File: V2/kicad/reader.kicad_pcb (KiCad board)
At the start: 2 copper layers, 42.5 x 62 mm, 93 parts, among them SW1 SW_Rezistance, SW2 SW_src, U1 STM32H523CET6, U2 MAX98357AETE+T, U3 MLD-TF PUSH-H18, U4 TCAN1057AVDRQ1, U5 ESD2CAN24-ES, U6 RJ-064-1, U7 MCP16301Hx-xCH, Y1 16MHz

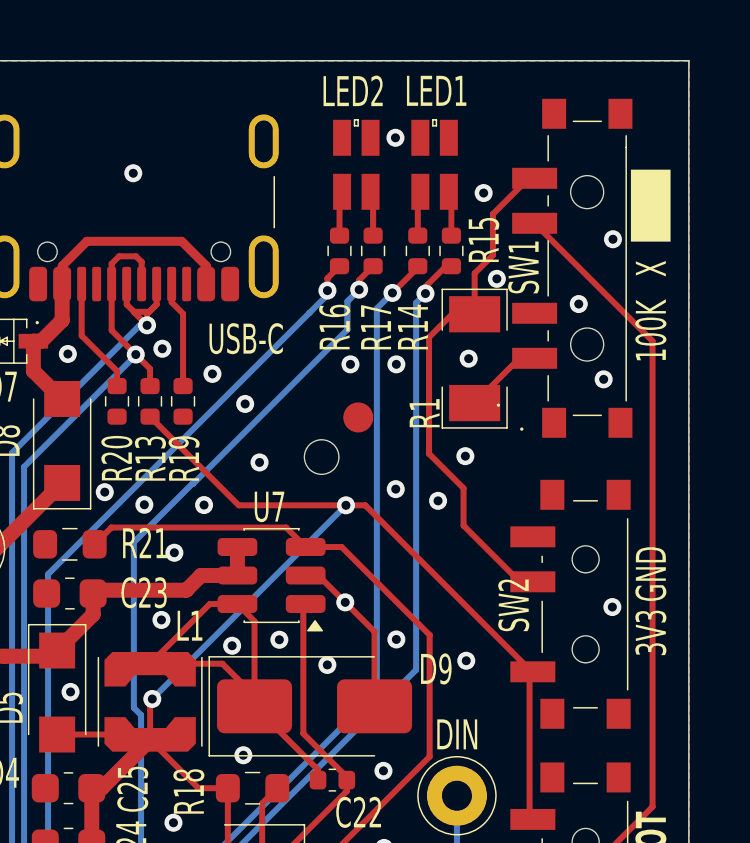
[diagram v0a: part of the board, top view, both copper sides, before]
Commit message: changed signage in gain slot table
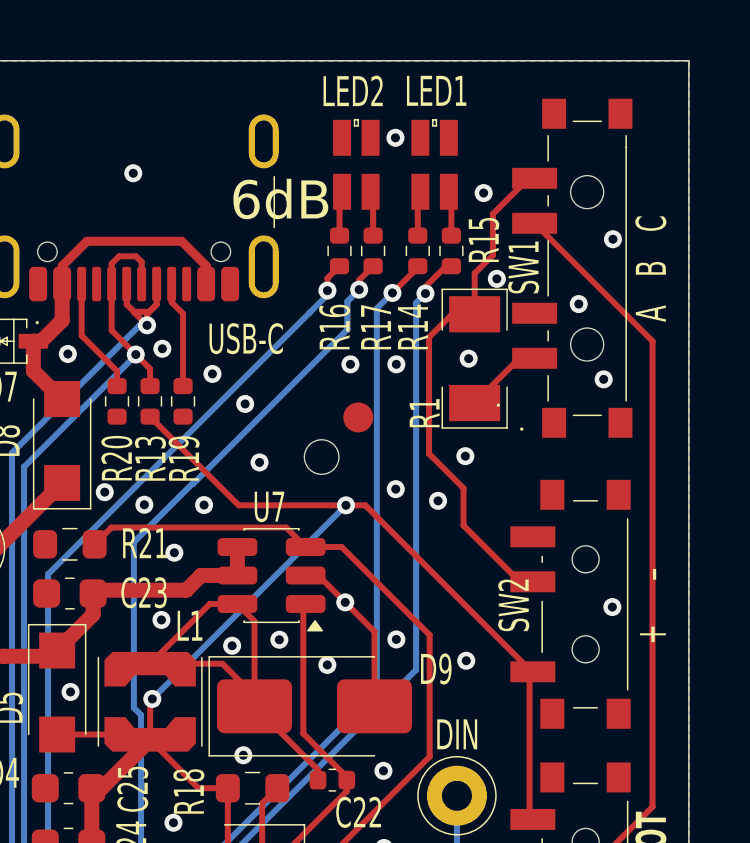
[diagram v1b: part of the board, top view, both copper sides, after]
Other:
- board text added: "+"
- board text added: "-"
- board text added: "6dB"
- board text added: "A"
- board text added: "B"
- board text added: "C"
- board text removed: "100K"
- board text removed: "3V3"
- board text removed: "GND"
- board text removed: "X"
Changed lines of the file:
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@@
 		(sheetname "/")
 		(sheetfile "reader.kicad_sch")
-		(units
-			(unit
-				(name "A")
-				(pins "2" "1" "3")
-			)
-		)
 		(attr smd)
 		(duplicate_pad_numbers_are_jumpers no)
@@
 		)
 		(fp_line
+			(start 0 3.4)
+			(end 0 1.6)
+			(stroke
+				(width 0.1)
+				(type default)
+			)
+			(layer "Dwgs.User")
+		)
+		(fp_line
 			(start 4.4 -2.45)
 			(end 4.4 2.1)
@@
 	)
 	(gr_rect
-		(start 173.5675 31.63)
-		(end 174.89 34.03)
-		(stroke
-			(width 0)
-			(type solid)
-		)
-		(fill yes)
-		(layer "F.SilkS")
-	)
-	(gr_rect
 		(start 136.36 63.09)
 		(end 136.84 73.86)
@@
 		(layer "Edge.Cuts")
 	)
-	(gr_text "X"
-		(at 174.27 34.93 90)
+	(gr_text "C"
+		(at 174.27 33.43 90)
 		(layer "F.SilkS" knockout)
 		(effects
@@
 		)
 	)
-	(gr_text "100K"
-		(at 174.27 37.02 90)
+	(gr_text "B"
+		(at 174.27 34.93 90)
 		(layer "F.SilkS" knockout)
 		(effects
@@
 		)
 	)
-	(gr_text "GND"
-		(at 174.27 45.11 90)
+	(gr_text "A"
+		(at 174.27 36.43 90)
 		(layer "F.SilkS" knockout)
 		(effects
@@
 		)
 	)
-	(gr_text "3V3\n"
-		(at 174.27 47.07 90)
+	(gr_text "+"
+		(at 174.27 47.119001 90)
 		(layer "F.SilkS" knockout)
 		(effects
@@
 		)
 	)
+	(gr_text "-"
+		(at 174.27 45.119001 90)
+		(layer "F.SilkS" knockout)
+		(effects
+			(font
+				(size 1 1)
+				(thickness 0.075)
+			)
+		)
+	)
+	(gr_text "6dB"
+		(at 161.9 32.67 0)
+		(layer "F.SilkS")
+		(effects
+			(font
+				(size 1.27 1.27)
+			)
+		)
+	)
 	(gr_text "https://github.com/ostertag/UACS"
 		(at 154.469519 65.849997 90)
@@
 	)
 	(table
-		(column_count 1)
+		(column_count 2)
 		(layer "B.SilkS")
 		(border
@@
 			)
 		)
-		(column_widths 16.306541)
-		(row_heights 3.15 3.15 4.225 3.15 3.15)
+		(column_widths 3.904256 5.767872)
+		(row_heights 3.15 3.15 3.15 3.15 3.15)
 		(cells
-			(table_cell "3dB = 3V3 100k"
-				(start 153.95 48.075)
-				(end 157.1 31.768459)
+			(table_cell "A+"
+				(start 155.425 46.096064)
+				(end 158.575 42.191808)
+				(margins 1.0025 1.0025 1.0025 1.0025)
+				(span 1 1)
+				(angle 90)
+				(layer "B.SilkS")
+				(effects
+					(font
+						(size 1 1)
+						(thickness 0.15)
+					)
+					(justify left mirror)
+				)
+			)
+			(table_cell "3dB\n"
+				(start 155.425 42.191808)
+				(end 158.575 36.423936)
 				(margins 1.0025 1.0025 1.0025 1.0025)
 				(span 1 1)
@@
 				)
 			)
-			(table_cell "6dB = 3V3"
-				(start 157.1 48.075)
-				(end 160.25 31.768459)
+			(table_cell "C+"
+				(start 158.575 46.096064)
+				(end 161.725 42.191808)
 				(margins 1.0025 1.0025 1.0025 1.0025)
 				(span 1 1)
@@
 				)
 			)
-			(table_cell "6dB = X"
-				(start 160.25 48.075)
-				(end 164.475 31.768459)
+			(table_cell "6dB"
+				(start 158.575 42.191808)
+				(end 161.725 36.423936)
 				(margins 1.0025 1.0025 1.0025 1.0025)
 				(span 1 1)
@@
 						(thickness 0.15)
 					)
-					(justify left bottom mirror)
+					(justify left mirror)
 				)
 			)
-			(table_cell "12dB = GND"
-				(start 164.475 48.075)
-				(end 167.625 31.768459)
+			(table_cell "B"
+				(start 161.725 46.096064)
+				(end 164.875 42.191808)
 				(margins 1.0025 1.0025 1.0025 1.0025)
 				(span 1 1)
@@
 				)
 			)
-			(table_cell "15dB = GND 100k"
-				(start 167.625 48.075)
-				(end 170.775 31.768459)
+			(table_cell "6dB"
+				(start 161.725 42.191808)
+				(end 164.875 36.423936)
+				(margins 1.0025 1.0025 1.0025 1.0025)
+				(span 1 1)
+				(angle 90)
+				(layer "B.SilkS")
+				(effects
+					(font
+						(size 1 1)
+						(thickness 0.15)
+					)
+					(justify left mirror)
+				)
+			)
+			(table_cell "C-"
+				(start 164.875 46.096064)
+				(end 168.025 42.191808)
+				(margins 1.0025 1.0025 1.0025 1.0025)
+				(span 1 1)
+				(angle 90)
+				(layer "B.SilkS")
+				(effects
+					(font
+						(size 1 1)
+						(thickness 0.15)
+					)
+					(justify left mirror)
+				)
+			)
+			(table_cell "12dB"
+				(start 164.875 42.191808)
+				(end 168.025 36.423936)
+				(margins 1.0025 1.0025 1.0025 1.0025)
+				(span 1 1)
+				(angle 90)
+				(layer "B.SilkS")
+				(effects
+					(font
+						(size 1 1)
+						(thickness 0.15)
+					)
+					(justify left mirror)
+				)
+			)
+			(table_cell "A-"
+				(start 168.025 46.096064)
+				(end 171.175 42.191808)
+				(margins 1.0025 1.0025 1.0025 1.0025)
+				(span 1 1)
+				(angle 90)
+				(layer "B.SilkS")
+				(effects
+					(font
+						(size 1 1)
+						(thickness 0.15)
+					)
+					(justify left mirror)
+				)
+			)
+			(table_cell "15dB"
+				(start 168.025 42.191808)
+				(end 171.175 36.423936)
 				(margins 1.0025 1.0025 1.0025 1.0025)
 				(span 1 1)
@@
 	)
 	(segment
+		(start 138.01 74.95)
+		(end 136.54 74.95)
+		(width 0.2)
+		(layer "F.Cu")
+		(net "Net-(U1-VDDA)")
+	)
+	(segment
+		(start 138.65 75.59)
+		(end 138.01 74.95)
+		(width 0.2)
+		(layer "F.Cu")
+		(net "Net-(U1-VDDA)")
+	)
+	(segment
+		(start 139.43595 73.28595)
+		(end 139.43595 75.00095)
+		(width 0.3)
+		(layer "F.Cu")
+		(net "Net-(U1-VDDA)")
+	)
+	(segment
+		(start 139.7329 72.989)
+		(end 139.43595 73.28595)
+		(width 0.3)
+		(layer "F.Cu")
+		(net "Net-(U1-VDDA)")
+	)
+	(segment
+		(start 140.8036 72.989)
+		(end 139.7329 72.989)
+		(width 0.3)
+		(layer "F.Cu")
+		(net "Net-(U1-VDDA)")
+	)
+	(segment
+		(start 139.43595 75.00095)
+		(end 140.21 75.775)
+		(width 0.3)
+		(layer "F.Cu")
+		(net "Net-(U1-VDDA)")
+	)
+	(segment
+		(start 138.65 75.59)
+		(end 138.8469 75.59)
+		(width 0.2)
+		(layer "F.Cu")
+		(net "Net-(U1-VDDA)")
+	)
+	(segment
+		(start 138.8469 75.59)
+		(end 139.43595 75.00095)
+		(width 0.2)
+		(layer "F.Cu")
+		(net "Net-(U1-VDDA)")
+	)
+	(segment
 		(start 164.51 35.63)
 		(end 164.51 35.314)
@@
 		(net "Net-(LED2-A2)")
 	)
-	(segment
-		(start 138.01 74.95)
-		(end 136.54 74.95)
-		(width 0.2)
-		(layer "F.Cu")
-		(net "Net-(U1-VDDA)")
-	)
-	(segment
-		(start 138.65 75.59)
-		(end 138.01 74.95)
-		(width 0.2)
-		(layer "F.Cu")
-		(net "Net-(U1-VDDA)")
-	)
-	(segment
-		(start 139.43595 73.28595)
-		(end 139.43595 75.00095)
-		(width 0.3)
-		(layer "F.Cu")
-		(net "Net-(U1-VDDA)")
-	)
-	(segment
-		(start 139.7329 72.989)
-		(end 139.43595 73.28595)
-		(width 0.3)
-		(layer "F.Cu")
-		(net "Net-(U1-VDDA)")
-	)
-	(segment
-		(start 140.8036 72.989)
-		(end 139.7329 72.989)
-		(width 0.3)
-		(layer "F.Cu")
-		(net "Net-(U1-VDDA)")
-	)
-	(segment
-		(start 139.43595 75.00095)
-		(end 140.21 75.775)
-		(width 0.3)
-		(layer "F.Cu")
-		(net "Net-(U1-VDDA)")
-	)
-	(segment
-		(start 138.65 75.59)
-		(end 138.8469 75.59)
-		(width 0.2)
-		(layer "F.Cu")
-		(net "Net-(U1-VDDA)")
-	)
-	(segment
-		(start 138.8469 75.59)
-		(end 139.43595 75.00095)
-		(width 0.2)
-		(layer "F.Cu")
-		(net "Net-(U1-VDDA)")
-	)
 	(zone

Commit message: fixed errors in board check: courtyard overlaps with fiducials
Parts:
- moved H2 1.87 mm to (161.4, 41.4)
- moved C21 1.66 mm to (160.7, 84.2)
- moved REF** 1.63 mm to (163.4, 83.3)
- moved REF** 1.25 mm to (145.0, 83.3)
- moved REF** 1.05 mm to (163.4, 39.9)
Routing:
- net +3.3V: track 186.3 -> 184.5 mm
- net Net-(SW2-B): track 16.5 -> 15.8 mm
- net /SPI_SCK: track 29.5 -> 30.1 mm
- net Net-(R1-Pad1): track 2.62 -> 2.11 mm
- net GND: vias 183 -> 182

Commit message: chore: small PCB layout changes
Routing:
- net /I2S_SDO: track 31.9 -> 32.5 mm
- net /RFID_SS: track 19.8 -> 19.2 mm
- net GND: vias 182 -> 187
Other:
- board text removed: "6dB"

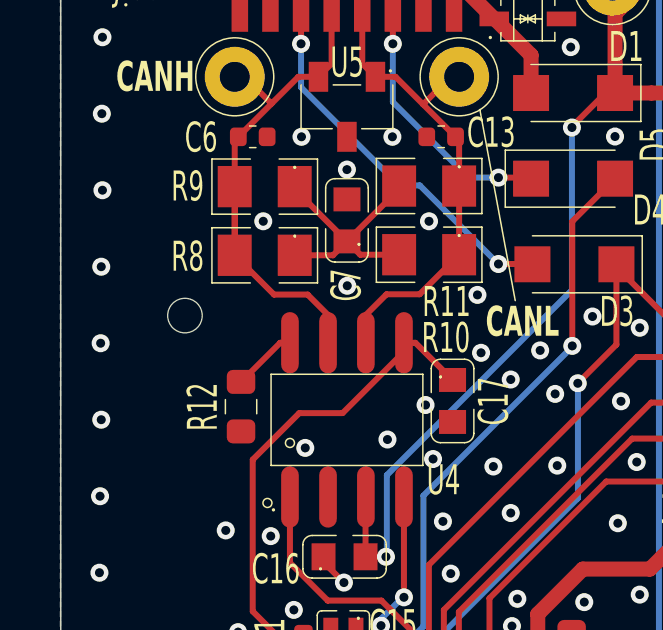
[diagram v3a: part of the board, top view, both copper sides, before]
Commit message: changed 20mA led to 2mA led so both are same. changed orientation of card logo on back of board
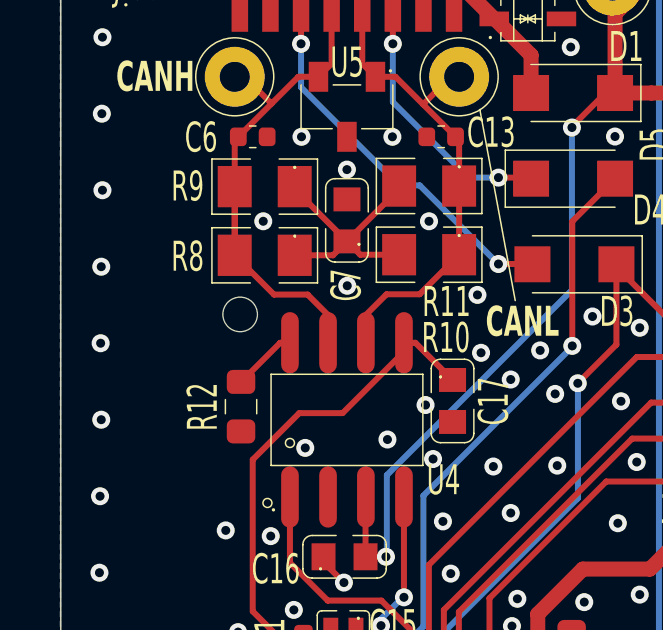
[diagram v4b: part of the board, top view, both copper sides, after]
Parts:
- LED2: value APHBM2012SURKCGKC -> APHBM2012LSURKZGKC
- R16: value 56 R -> 330 R
- R17: value 68 R -> 560 R
- moved G*** 2.50 mm to (162.1, 72.3)
- moved G*** 2.50 mm to (138.1, 54.0), turned to -90 degrees
- moved G*** 2.50 mm to (147.7, 63.4)
- moved H1 1.84 mm to (139.0, 55.2)
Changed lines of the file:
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@@
 			(layers "F.Cu" "F.Mask" "F.Paste")
 			(roundrect_rratio 0.25)
-			(net "Net-(U1-VDDA)")
+			(net "/Net-(U1-VDDA)")
 			(pintype "passive")
 		)
@@
 			)
 		)
-		(property "Value" "68 R"
+		(property "Value" "560 R"
 			(at 0 1.17 90)
 			(layer "F.Fab")
@@
 			)
 		)
-		(property "Datasheet" "https://jlcpcb.com/api/file/downloadByFileSystemAccessId/8588908782960693248"
+		(property "Datasheet" "https://jlc-prod-smt.oss-eu-central-1.aliyuncs.com/smtDataManualFile/8586178278474862592-C25126.pdf?response-content-disposition=attachment%3B%20filename%3DC25126.pdf%3B%20filename%2A%3DUTF-8%27%27C25126.pdf&x-oss-date=20260603T141942Z&x-oss-expires=1800&x-oss-security-token=CAISgAN1q6Ft5B2yfSjIr5rYAPaHqJFCjrvadU%2FFs1YWQtlZrr3lsTz2IHhMdHJsAOodtv0%2FmmhT6PkclqRLcbhpcmfjV%2BZHzLB8qeAa7RNB4J7b16cNrbH4M4H6aXeirtuwDsz9SNTCALjPD3nPii50x5bjaDymRCbLGJaViJlhHLN1Ow6jdmhpCctxLAlvo9NgFxm3D%2Fu2NQPwiWf9FVdhvhEG6Vly8qOi2MaRmFy8yFTx0b0SvJ%2BjYMrmPctoN9JnSdC5mfdzau3a1TJ84gRD0a5wkaVA1zbDs5bfISEIuUzebreLqY03dV4mOvdqIcMe8qigz88fk%2FfIioH6xyxKOexoSCnFTOiiupCcQLPyao9jLu6iayqViY7QaIOTqQohZmkAMwVOasAsI3Ngh4zF97Qt0cVNkXO9gWfLI8DtuMleWhqDHsNdntHD0eS19jklBdzSlusJRAJJUVBflCeKEaRNSAd3WGhEfM2%2BBt4QT30w5N2u00S8OSMIe8fo%2BKKWD5sagAFAjLTD0371Sd2gSdBnykA7MII9CzBs0TEnncOuMMFpZ7eWxtofkMZUw83MXKFT3yGfjS9fIlx%2Bre7vtwbXSVmucxBbZSJldeqhHVomhZC6FwsraIa5cFo%2FJ2rvy%2BYXQ1kdyLEoPt0fplni6hRiSJOL598AUZr9EPV4uuEaQBdebyAA&x-oss-signature-version=OSS4-HMAC-SHA256&x-oss-credential=STS.NYmKL3ENc9y1witWVCNVuAxNS%2F20260603%2Feu-central-1%2Foss%2Faliyun_v4_request&x-oss-signature=d1629a371fbf831c62f9f7f4032d37edb65e47d37709e76674d141769ad7b5bf"
 			(at 0 0 90)
 			(layer "F.Fab")
@@
 			)
 		)
-		(property "JLCPCB" "https://jlcpcb.com/partdetail/Yageo-RC0402FR0768RL/C163455"
+		(property "JLCPCB" "https://jlcpcb.com/partdetail/C25126"
 			(at 0 0 90)
 			(unlocked yes)
@@
 			)
 		)
-		(property "LCSC" "C163455"
+		(property "LCSC" "C25126"
 			(at 0 0 90)
 			(unlocked yes)
@@
 			(layers "F.Cu" "F.Mask" "F.Paste")
 			(roundrect_rratio 0.25)
-			(net "Net-(U1-VDDA)")
+			(net "/Net-(U1-VDDA)")
 			(pintype "passive")
 		)
@@
 			(layers "F.Cu" "F.Mask" "F.Paste")
 			(roundrect_rratio 0.25)
-			(net "Net-(U1-VDDA)")
+			(net "/Net-(U1-VDDA)")
 			(pintype "passive")
 		)
@@
 	(footprint "MountingHole:ToolingHole_1.152mm"
 		(layer "F.Cu")
-		(at 137.14 55.269 180)
+		(at 138.98 55.23 180)
 		(descr "Tooling Hole 1.152mm, 1.3mm solder mask, JLCPCB specification, https://jlcpcb.com/help/article/How-to-add-tooling-holes-for-PCB-assembly-order")
 		(tags "mounting")
@@
 			(polygon
 				(pts
-					(xy 136.44 55.269) (xy 136.460341 55.436521) (xy 136.520181 55.594306) (xy 136.616042 55.733186)
-					(xy 136.742355 55.845089) (xy 136.891777 55.923511) (xy 137.055624 55.963896) (xy 137.224376 55.963896)
-					(xy 137.388223 55.923511) (xy 137.537645 55.845089) (xy 137.663958 55.733186) (xy 137.759819 55.594306)
-					(xy 137.819659 55.436521) (xy 137.84 55.269) (xy 137.819659 55.101479) (xy 137.759819 54.943694)
-					(xy 137.663958 54.804814) (xy 137.537645 54.692911) (xy 137.388223 54.614489) (xy 137.224376 54.574104)
-					(xy 137.055624 54.574104) (xy 136.891777 54.614489) (xy 136.742355 54.692911) (xy 136.616042 54.804814)
-					(xy 136.520181 54.943694) (xy 136.460341 55.101479)
+					(xy 138.28 55.23) (xy 138.300341 55.397521) (xy 138.360181 55.555306) (xy 138.456042 55.694186)
+					(xy 138.582355 55.806089) (xy 138.731777 55.884511) (xy 138.895624 55.924896) (xy 139.064376 55.924896)
+					(xy 139.228223 55.884511) (xy 139.377645 55.806089) (xy 139.503958 55.694186) (xy 139.599819 55.555306)
+					(xy 139.659659 55.397521) (xy 139.68 55.23) (xy 139.659659 55.062479) (xy 139.599819 54.904694)
+					(xy 139.503958 54.765814) (xy 139.377645 54.653911) (xy 139.228223 54.575489) (xy 139.064376 54.535104)
+					(xy 138.895624 54.535104) (xy 138.731777 54.575489) (xy 138.582355 54.653911) (xy 138.456042 54.765814)
+					(xy 138.360181 54.904694) (xy 138.300341 55.062479)
 				)
 			)
@@
 			(size 0.2794 1.461999)
 			(layers "F.Cu" "F.Mask" "F.Paste")
-			(net "Net-(U1-VDDA)")
+			(net "/Net-(U1-VDDA)")
 			(pinfunction "VDDA_9")
 			(pintype "power_in")
@@
 		(sheetname "/")
 		(sheetfile "reader.kicad_sch")
+		(units
+			(unit
+				(name "A")
+				(pins "2" "1" "3")
+			)
+		)
 		(attr smd)
 		(duplicate_pad_numbers_are_jumpers no)
@@
 			)
 		)
-		(property "Value" "APHBM2012SURKCGKC"
+		(property "Value" "APHBM2012LSURKZGKC"
 			(at -0.05 2.6 0)
 			(layer "F.Fab")
@@
 			)
 		)
-		(property "Datasheet" "https://jlcpcb.com/api/file/downloadByFileSystemAccessId/8590902847586181120"
+		(property "Datasheet" "https://jlcpcb.com/api/file/downloadByFileSystemAccessId/8590908716709863424"
 			(at 0 0 180)
 			(unlocked yes)
@@
 			)
 		)
-		(property "JLCPCB" "https://jlcpcb.com/partdetail/Kingbright-APHBM2012SURKCGKC/C5553822"
+		(property "JLCPCB" "https://jlcpcb.com/partdetail/Kingbright-APHBM2012LSURKZGKC/C6465979"
 			(at 0 0 180)
 			(unlocked yes)
@@
 			)
 		)
-		(property "LCSC" "C5553822"
+		(property "LCSC" "C6465979"
 			(at 0 0 180)
 			(unlocked yes)
@@
 			)
 		)
-		(property "Note" "20mA, Red, Emerald, 120°, SMD-4P, 2 x 1.3 mm"
+		(property "Note" "2mA Red, Emerald, 120°, SMD-4P, 2 x 1.3 mm"
 			(at 0 0 180)
 			(unlocked yes)
@@
 			)
 		)
-		(property "Value" "56 R"
+		(property "Value" "330 R"
 			(at 0 1.17 90)
 			(layer "F.Fab")
@@
 			)
 		)
-		(property "Datasheet" "https://jlcpcb.com/api/file/downloadByFileSystemAccessId/8586178279397068800"
+		(property "Datasheet" "https://jlcpcb.com/api/file/downloadByFileSystemAccessId/8579706017514917888"
 			(at 0 0 90)
 			(layer "F.Fab")
@@
 			)
 		)
-		(property "JLCPCB" "https://jlcpcb.com/partdetail/25870-0402WGF560JTCE/C25127"
+		(property "JLCPCB" "https://jlcpcb.com/partdetail/25847-0402WGF3300TCE/C25104"
 			(at 0 0 90)
 			(unlocked yes)
@@
 			)
 		)
-		(property "LCSC" "C25127"
+		(property "LCSC" "C25104"
 			(at 0 0 90)
 			(unlocked yes)
@@
 	(footprint "LOGO"
 		(layer "B.Cu")
-		(at 162.05 74.826807 -90)
+		(at 162.05 72.326807 -90)
 		(property "Reference" "G***"
 			(at 0 0 90)
@@
 	(footprint "LOGO"
 		(layer "B.Cu")
-		(at 138.07 56.5 90)
+		(at 138.07 54 -90)
 		(property "Reference" "G***"
 			(at 0 0 90)
@@
 	(footprint "LOGO"
 		(layer "B.Cu")
-		(at 147.65 65.85 -90)
+		(at 147.65 63.35 -90)
 		(property "Reference" "G***"
 			(at 0 0 90)
@@
 	)
 	(gr_rect
-		(start 136.36 63.09)
-		(end 136.84 73.86)
+		(start 136.36 60.59)
+		(end 136.84 71.36)
 		(stroke
 			(width 0.1)
@@
 	)
 	(gr_rect
-		(start 136.36 63.09)
-		(end 141.21 63.35)
+		(start 136.36 60.59)
+		(end 141.21 60.85)
 		(stroke
 			(width 0.1)
@@
 	)
 	(gr_rect
-		(start 136.36 63.09)
-		(end 141.36 73.84)
+		(start 136.36 60.59)
+		(end 141.36 71.34)
 		(stroke
 			(width 0.5)
@@
 	)
 	(gr_rect
-		(start 138.24 63.04)
-		(end 139.21 73.84)
+		(start 138.24 60.54)
+		(end 139.21 71.34)
 		(stroke
 			(width 0.1)
@@
 	)
 	(gr_rect
-		(start 138.99 63)
-		(end 141.3 63.5)
+		(start 138.99 60.5)
+		(end 141.3 61)
 		(stroke
 			(width 0.1)
@@
 	)
 	(gr_rect
-		(start 138.99 73.46)
-		(end 141.3 73.96)
+		(start 138.99 70.96)
+		(end 141.3 71.46)
 		(stroke
 			(width 0.1)
@@
 	)
 	(gr_rect
-		(start 140.87 63.07)
-		(end 141.35 73.84)
+		(start 140.87 60.57)
+		(end 141.35 71.34)
 		(stroke
 			(width 0.1)
@@
 	)
 	(gr_text "https://github.com/ostertag/UACS"
-		(at 154.469519 65.849997 90)
+		(at 154.469519 63.349997 90)
 		(layer "B.SilkS")
 		(effects
@@
 	)
 	(gr_text "UACS-Reader"
-		(at 137.01 68.465 90)
+		(at 137.01 65.965 90)
 		(layer "B.SilkS" knockout)
 		(effects
@@
 	)
 	(gr_text "2.0 2026/06"
-		(at 140.01 68.465 90)
+		(at 140.01 65.965 90)
 		(layer "B.SilkS" knockout)
 		(effects
@@
 	)
 	(segment
-		(start 138.01 74.95)
-		(end 136.54 74.95)
-		(width 0.2)
-		(layer "F.Cu")
-		(net "Net-(U1-VDDA)")
-	)
-	(segment
-		(start 138.65 75.59)
-		(end 138.01 74.95)
-		(width 0.2)
-		(layer "F.Cu")
-		(net "Net-(U1-VDDA)")
-	)
-	(segment
-		(start 139.43595 73.28595)
-		(end 139.43595 75.00095)
-		(width 0.3)
-		(layer "F.Cu")
-		(net "Net-(U1-VDDA)")
-	)
-	(segment
-		(start 139.7329 72.989)
-		(end 139.43595 73.28595)
-		(width 0.3)
-		(layer "F.Cu")
-		(net "Net-(U1-VDDA)")
-	)
-	(segment
-		(start 140.8036 72.989)
-		(end 139.7329 72.989)
-		(width 0.3)
-		(layer "F.Cu")
-		(net "Net-(U1-VDDA)")
-	)
-	(segment
-		(start 139.43595 75.00095)
-		(end 140.21 75.775)
-		(width 0.3)
-		(layer "F.Cu")
-		(net "Net-(U1-VDDA)")
-	)
-	(segment
-		(start 138.65 75.59)
-		(end 138.8469 75.59)
-		(width 0.2)
-		(layer "F.Cu")
-		(net "Net-(U1-VDDA)")
-	)
-	(segment
-		(start 138.8469 75.59)
-		(end 139.43595 75.00095)
-		(width 0.2)
-		(layer "F.Cu")
-		(net "Net-(U1-VDDA)")
-	)
-	(segment
 		(start 164.51 35.63)
 		(end 164.51 35.314)
@@
 		(net "Net-(LED2-A2)")
 	)
+	(segment
+		(start 138.01 74.95)
+		(end 136.54 74.95)
+		(width 0.2)
+		(layer "F.Cu")
+		(net "/Net-(U1-VDDA)")
+	)
+	(segment
+		(start 138.65 75.59)
+		(end 138.01 74.95)
+		(width 0.2)
+		(layer "F.Cu")
+		(net "/Net-(U1-VDDA)")
+	)
+	(segment
+		(start 139.43595 73.28595)
+		(end 139.43595 75.00095)
+		(width 0.3)
+		(layer "F.Cu")
+		(net "/Net-(U1-VDDA)")
+	)
+	(segment
+		(start 139.7329 72.989)
+		(end 139.43595 73.28595)
+		(width 0.3)
+		(layer "F.Cu")
+		(net "/Net-(U1-VDDA)")
+	)
+	(segment
+		(start 140.8036 72.989)
+		(end 139.7329 72.989)
+		(width 0.3)
+		(layer "F.Cu")
+		(net "/Net-(U1-VDDA)")
+	)
+	(segment
+		(start 139.43595 75.00095)
+		(end 140.21 75.775)
+		(width 0.3)
+		(layer "F.Cu")
+		(net "/Net-(U1-VDDA)")
+	)
+	(segment
+		(start 138.65 75.59)
+		(end 138.8469 75.59)
+		(width 0.2)
+		(layer "F.Cu")
+		(net "/Net-(U1-VDDA)")
+	)
+	(segment
+		(start 138.8469 75.59)
+		(end 139.43595 75.00095)
+		(width 0.2)
+		(layer "F.Cu")
+		(net "/Net-(U1-VDDA)")
+	)
 	(zone
